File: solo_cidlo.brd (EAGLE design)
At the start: 30 x 10 mm, 4 parts, among them Q1 QRD1114

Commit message: Add files via upload
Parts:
- moved R1 2.50 mm to (27.5, 4.00)
- moved R2 2.50 mm to (27.5, 6.00)
- flipped S1 to the bottom, turned to 270 degrees
- renumbered Q1 to S1
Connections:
- removed net N$3: JP2.1, R1.2, R2.2
- removed net N$4: JP2.3, S1.P$2, S1.P$4
- new net +5V: JP2.2, R1.2, R2.2
- new net GND: JP2.3, S1.P$2, S1.P$4
- net N$2: now also JP2.1; no longer JP2.2
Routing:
- net N$4: track 26.4 -> 0.00 mm
- net N$3: track 19.2 -> 0.00 mm
- net N$2: track 23.6 -> 25.0 mm, vias 2 -> 1
- added copper zone on layer 1, net +5V
- removed copper zone on layer 1, net GND
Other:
- board text added: "GND"
- board text added: "S1"
- board text added: "VCC"
- board text added: "°"

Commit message: Add files via upload
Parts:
- added LED1: (no value), led:CHIPLED_0603
- added R3: 330, resistor:R0201
- moved JP2 0.25 mm to (43.8, 5.00)
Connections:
- net N$1 renamed IL1
- net N$2 renamed S1
- new net KL1: LED1.A, R3.1
- net +5V: now also R3.2
- net GND: now also LED1.C
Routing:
- net +5V: track 0.00 -> 6.34 mm
- net GND: track 0.00 -> 2.92 mm, vias 0 -> 1
- net KL1: track 0.00 -> 0.87 mm
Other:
- board size 30 x 10 mm -> 41 x 10 mm
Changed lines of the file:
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@@
 <setting verticaltext="up"/>
 </settings>
-<grid distance="1" unitdist="mm" unit="mm" style="lines" multiple="1" display="yes" altdistance="0.25" altunitdist="mm" altunit="mm"/>
+<grid distance="1" unitdist="mm" unit="mm" style="lines" multiple="1" display="yes" altdistance="0.125" altunitdist="mm" altunit="mm"/>
 <layers>
 <layer number="1" name="Top" color="4" fill="1" visible="yes" active="yes"/>
@@
 <layer number="43" name="vRestrict" color="2" fill="10" visible="yes" active="yes"/>
 <layer number="44" name="Drills" color="7" fill="1" visible="no" active="yes"/>
-<layer number="45" name="Holes" color="7" fill="1" visible="no" active="yes"/>
+<layer number="45" name="Holes" color="7" fill="1" visible="yes" active="yes"/>
 <layer number="46" name="Milling" color="3" fill="1" visible="no" active="yes"/>
 <layer number="47" name="Measures" color="7" fill="1" visible="no" active="yes"/>
@@
 <board>
 <plain>
-<wire x1="17" y1="0" x2="47" y2="0" width="0" layer="20"/>
-<wire x1="47" y1="0" x2="47" y2="10" width="0" layer="20"/>
-<wire x1="47" y1="10" x2="17" y2="10" width="0" layer="20"/>
-<wire x1="17" y1="10" x2="17" y2="0" width="0" layer="20"/>
+<wire x1="13" y1="0" x2="54" y2="0" width="0" layer="20"/>
+<wire x1="54" y1="0" x2="54" y2="10" width="0" layer="20"/>
+<wire x1="54" y1="10" x2="13" y2="10" width="0" layer="20"/>
+<wire x1="13" y1="10" x2="13" y2="0" width="0" layer="20"/>
 <text x="42" y="8.25" size="1.778" layer="37" rot="R180">GND</text>
 <text x="42" y="5.75" size="1.778" layer="37" rot="R180">VCC</text>
 <text x="42" y="3.25" size="1.778" layer="37" rot="R180">S1</text>
-<text x="25" y="1" size="1.778" layer="37">°</text>
+<text x="25" y="6.25" size="1.778" layer="37">°</text>
+<hole x="16" y="5" drill="3"/>
+<hole x="51" y="5" drill="3"/>
+<text x="22.75" y="2.5" size="1" layer="51" rot="R180">S1</text>
+<text x="26" y="6.25" size="1.778" layer="52" rot="MR0">°</text>
+<text x="46" y="1.875" size="1.75" layer="51">°</text>
 </plain>
 <attributes>
@@
 </element>
 <element name="R2" library="resistor" library_urn="urn:adsk.eagle:library:348" package="MINI_MELF-0102W" package3d_urn="urn:adsk.eagle:package:26105/1" value="10 k" x="27.5" y="6" smashed="yes">
-<attribute name="NAME" x="29.23" y="5.4525" size="1.27" layer="25"/>
-</element>
-<element name="JP2" library="pinhead" library_urn="urn:adsk.eagle:library:325" package="1X03" package3d_urn="urn:adsk.eagle:package:22458/2" value="" x="44" y="5" smashed="yes" rot="R90">
-<attribute name="VALUE" x="47.175" y="1.19" size="1.27" layer="27" rot="R90"/>
+<attribute name="NAME" x="28.98" y="5.4525" size="1.27" layer="25"/>
+</element>
+<element name="JP2" library="pinhead" library_urn="urn:adsk.eagle:library:325" package="1X03" package3d_urn="urn:adsk.eagle:package:22458/2" value="" x="43.75" y="5" smashed="yes" rot="R90">
+<attribute name="VALUE" x="46.925" y="1.19" size="1.27" layer="27" rot="R90"/>
+</element>
+<element name="LED1" library="led" library_urn="urn:adsk.eagle:library:259" package="CHIPLED_0603" package3d_urn="urn:adsk.eagle:package:15822/2" value="" x="46.5" y="5" smashed="yes" rot="R180">
+<attribute name="NAME" x="47.135" y="6.52" size="0.8" layer="25" rot="R270"/>
+<attribute name="VALUE" x="44.595" y="6.27" size="1.27" layer="27" rot="R270"/>
+</element>
+<element name="R3" library="resistor" library_urn="urn:adsk.eagle:library:348" package="R0201" package3d_urn="urn:adsk.eagle:package:26117/1" value="330" x="46.5" y="6.875" smashed="yes" rot="R90">
+<attribute name="NAME" x="46.9225" y="7.23" size="0.8" layer="25" rot="R90"/>
 </element>
 </elements>
 <signals>
-<signal name="N$1">
+<signal name="IL1">
 <contactref element="S1" pad="P$3"/>
 <contactref element="R1" pad="1"/>
@@
 <wire x1="23.3368" y1="4" x2="23.27" y2="3.9332" width="1.016" layer="1"/>
 </signal>
-<signal name="N$2">
+<signal name="S1">
 <contactref element="S1" pad="P$1"/>
 <contactref element="R2" pad="1"/>
@@
 <wire x1="25" y1="6.0414" x2="25" y2="4" width="1.016" layer="16"/>
 <wire x1="25" y1="4" x2="26.54" y2="2.46" width="1.016" layer="16"/>
-<wire x1="26.54" y1="2.46" x2="44" y2="2.46" width="1.016" layer="16"/>
+<wire x1="26.54" y1="2.46" x2="43.75" y2="2.46" width="1.016" layer="16"/>
 </signal>
 <signal name="GND">
 <polygon width="0.1524" layer="16">
-<vertex x="15" y="12"/>
-<vertex x="15" y="-2"/>
-<vertex x="49" y="-2"/>
-<vertex x="49" y="12"/>
+<vertex x="19" y="10"/>
+<vertex x="19" y="0"/>
+<vertex x="49.5" y="0"/>
+<vertex x="49.5" y="10"/>
 </polygon>
 <contactref element="S1" pad="P$4"/>
 <contactref element="S1" pad="P$2"/>
 <contactref element="JP2" pad="3"/>
+<wire x1="43.75" y1="7.54" x2="44.46" y2="7.54" width="2.54" layer="16"/>
+<wire x1="43.75" y1="7.54" x2="42.54" y2="7.54" width="2.54" layer="16"/>
+<contactref element="LED1" pad="C"/>
+<wire x1="46.5" y1="4.25" x2="46.5" y2="3.25" width="0.8128" layer="1"/>
+<via x="46.5" y="3.25" extent="1-16" drill="0.35"/>
 </signal>
 <signal name="+5V">
@@
 <contactref element="R1" pad="2"/>
 <polygon width="0.1524" layer="1">
-<vertex x="16" y="11"/>
-<vertex x="16" y="-1"/>
-<vertex x="48" y="-1"/>
-<vertex x="48" y="11"/>
+<vertex x="19" y="10"/>
+<vertex x="19" y="0"/>
+<vertex x="49.5" y="0"/>
+<vertex x="49.5" y="10"/>
 </polygon>
+<wire x1="28.45" y1="6" x2="30" y2="6" width="1.016" layer="1"/>
+<wire x1="28.45" y1="4" x2="30" y2="4" width="1.016" layer="1"/>
+<wire x1="28.45" y1="4" x2="27.7184" y2="4" width="1.016" layer="1"/>
+<wire x1="28.45" y1="6" x2="28" y2="6" width="1.016" layer="1"/>
+<wire x1="43.75" y1="5" x2="42.5" y2="5" width="2.54" layer="1"/>
+<wire x1="43.75" y1="5" x2="44.5612125" y2="5" width="2.54" layer="1"/>
+<contactref element="R3" pad="2"/>
+</signal>
+<signal name="KL1">
+<contactref element="R3" pad="1"/>
+<contactref element="LED1" pad="A"/>
+<wire x1="46.5" y1="6.62" x2="46.5" y2="5.75" width="0.45" layer="1"/>
 </signal>
 </signals>

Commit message: Add files via upload
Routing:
- net +5V: track 6.34 -> 2.06 mm
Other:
- board text added: "QRD_1114-solo_0,1"
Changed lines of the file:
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@@
 <text x="26" y="6.25" size="1.778" layer="52" rot="MR0">°</text>
 <text x="46" y="1.875" size="1.75" layer="51">°</text>
+<text x="49" y="4" size="1.778" layer="52" rot="MR0">QRD_1114-solo_0,1</text>
+<text x="24" y="1" size="1.15" layer="51">QRD_1114-solo_0,1</text>
 </plain>
 <attributes>
@@
 <vertex x="19" y="10"/>
 <vertex x="19" y="0"/>
-<vertex x="49.5" y="0"/>
-<vertex x="49.5" y="10"/>
+<vertex x="48.5" y="0"/>
+<vertex x="48.5" y="10"/>
 </polygon>
 <contactref element="S1" pad="P$4"/>
@@
 <vertex x="19" y="10"/>
 <vertex x="19" y="0"/>
-<vertex x="49.5" y="0"/>
-<vertex x="49.5" y="10"/>
+<vertex x="48.5" y="0"/>
+<vertex x="48.5" y="10"/>
 </polygon>
-<wire x1="28.45" y1="6" x2="30" y2="6" width="1.016" layer="1"/>
-<wire x1="28.45" y1="4" x2="30" y2="4" width="1.016" layer="1"/>
-<wire x1="28.45" y1="4" x2="27.7184" y2="4" width="1.016" layer="1"/>
-<wire x1="28.45" y1="6" x2="28" y2="6" width="1.016" layer="1"/>
 <wire x1="43.75" y1="5" x2="42.5" y2="5" width="2.54" layer="1"/>
 <wire x1="43.75" y1="5" x2="44.5612125" y2="5" width="2.54" layer="1"/>

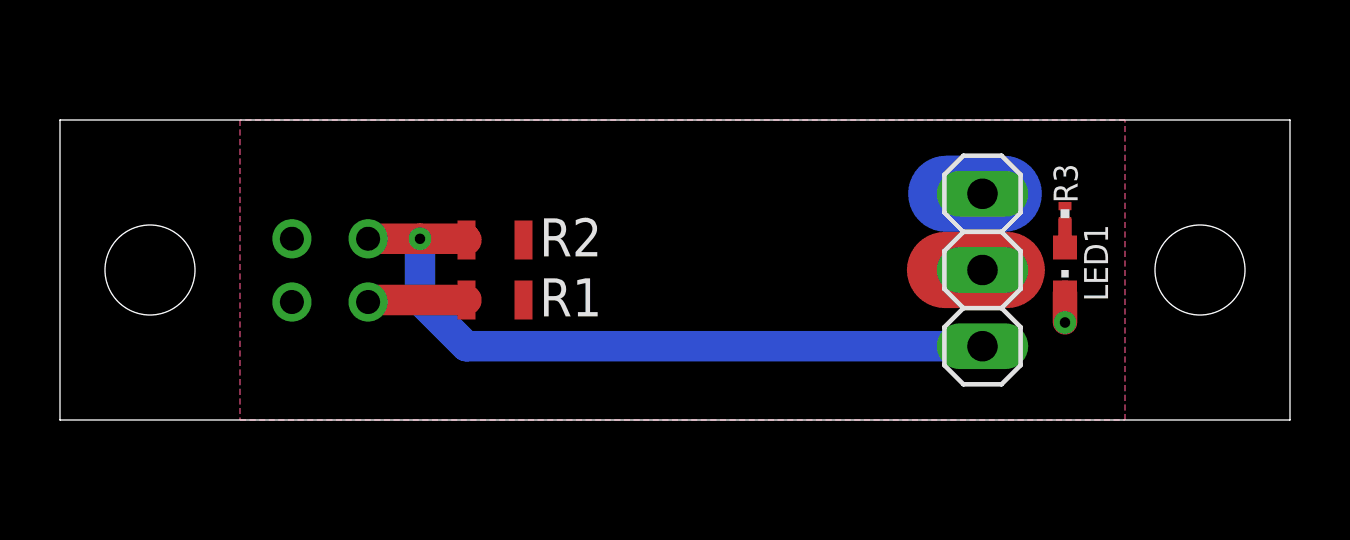
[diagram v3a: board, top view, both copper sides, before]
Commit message: Prepare PCB to manufacturing
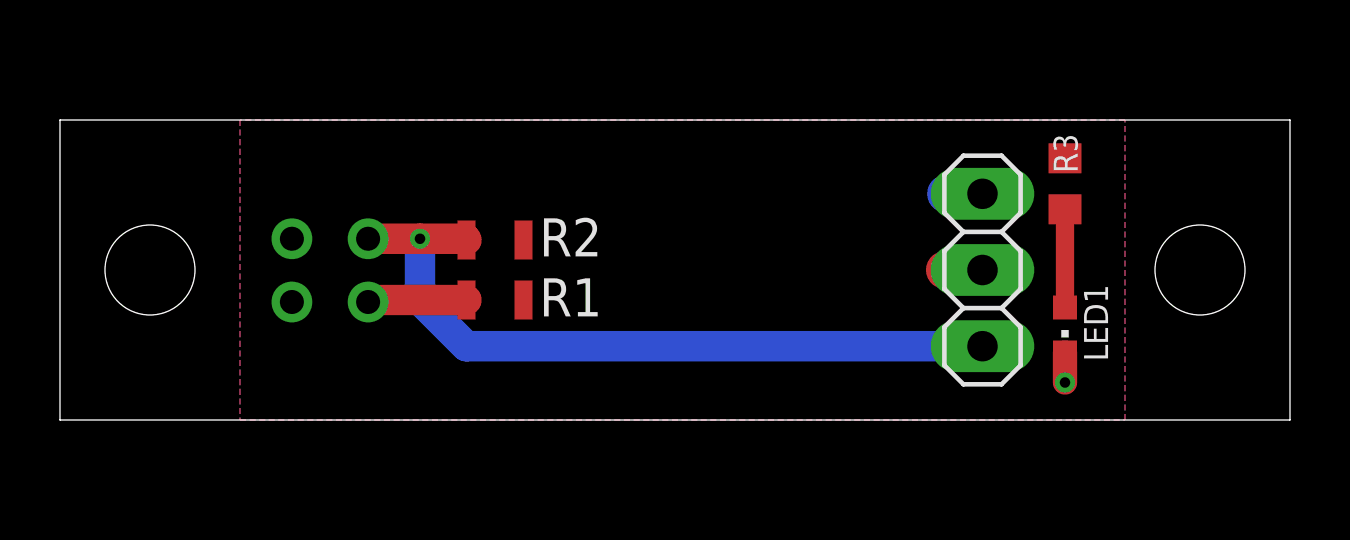
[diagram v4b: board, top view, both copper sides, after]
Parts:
- R3: device resistor:R0201 -> resistor:R0603
- moved LED1 2.00 mm to (46.5, 3.00)
- moved R3 1.00 mm to (46.5, 7.88)
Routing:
- net KL1: track 0.87 -> 3.28 mm
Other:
- board text added: "QRD1114-solo v1.0"
- board text added: "TVavrinec"
- board text removed: "QRD_1114-solo_0,1"
